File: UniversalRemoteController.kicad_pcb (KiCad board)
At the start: 8 copper layers, 92 parts, among them J1 USB_C_Receptacle_USB2.0_16P, J2 Conn_01x03_Pin, U1 USBLC6-2SC6, U2 TPS631000DRLR, U3 BQ25620RYKR, U4 STM32H750IBKx, U5 MAX16054AZT, U6 AP2161W

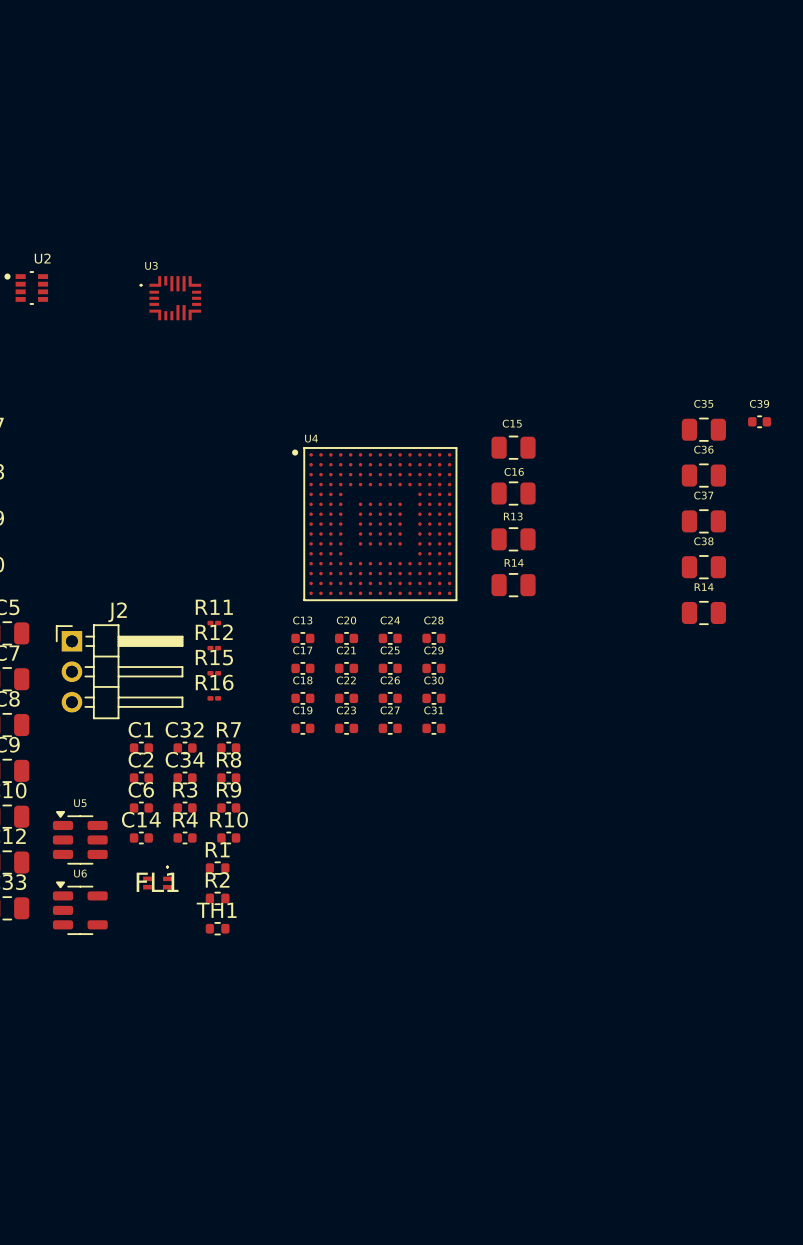
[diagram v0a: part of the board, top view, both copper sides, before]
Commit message: Add the SDRAM ic
16MB SDRAM add
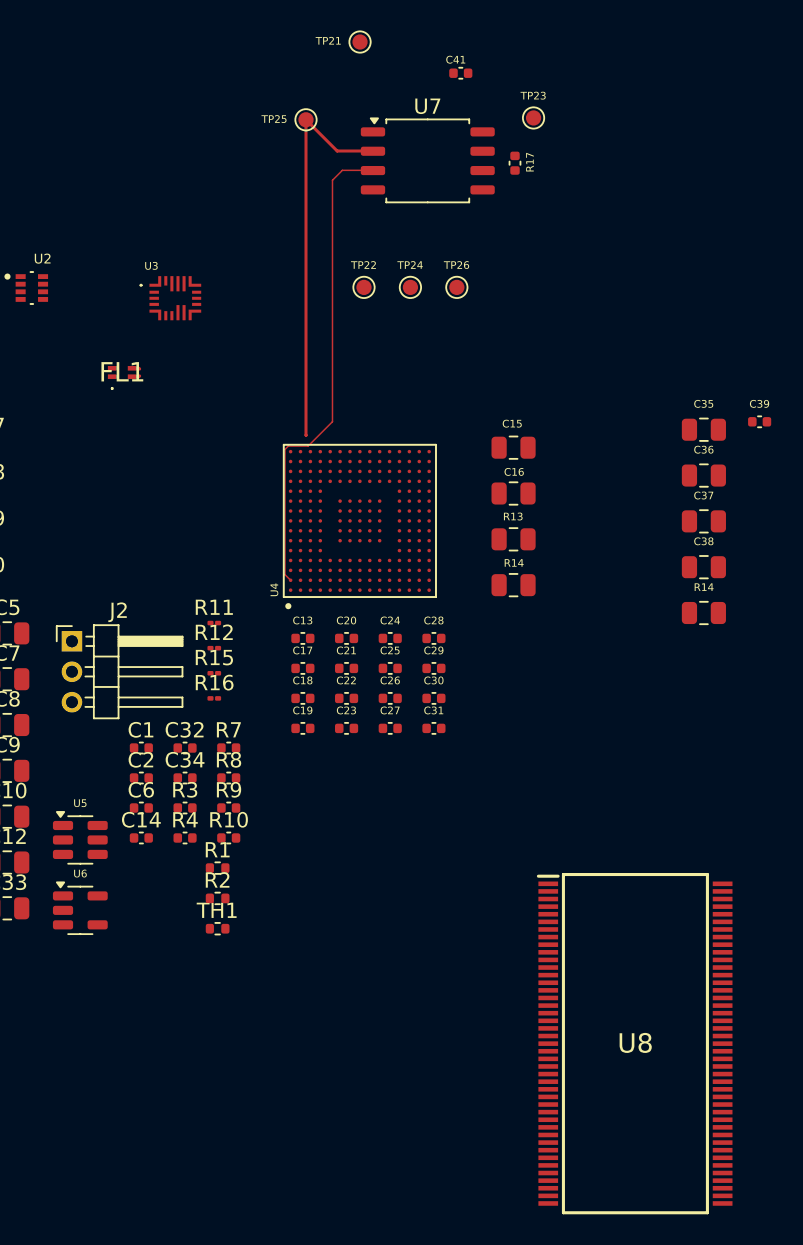
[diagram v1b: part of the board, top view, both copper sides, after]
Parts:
- added C41: 100n, Capacitor_SMD:C_0402_1005Metric, F.Cu at (137.0, 29.2)
- added R17: 10k, Capacitor_SMD:C_0402_1005Metric, F.Cu at (140.5, 35.2)
- added TP21: TestPoint, TestPoint:TestPoint_Pad_D1.0mm, F.Cu at (130.3, 27.2)
- added TP22: TestPoint, TestPoint:TestPoint_Pad_D1.0mm, F.Cu at (130.6, 43.3)
- added TP23: TestPoint, TestPoint:TestPoint_Pad_D1.0mm, F.Cu at (141.8, 32.2)
- added TP24: TestPoint, TestPoint:TestPoint_Pad_D1.0mm, F.Cu at (133.7, 43.3)
- added TP25: TestPoint, TestPoint:TestPoint_Pad_D1.0mm, F.Cu at (126.8, 32.3)
- added TP26: TestPoint, TestPoint:TestPoint_Pad_D1.0mm, F.Cu at (136.7, 43.3)
- added U7: W25Q128JVS, UniversalRemoteControllerLibrary:SOIC-8_5.23x5.23mm_P1.27mm, F.Cu at (134.8, 35.0)
- added U8: IS42S32400F-6TLI, UniversalRemoteControllerLibrary:SOP50P1176X120-86N, F.Cu at (148.4, 93.0)
- moved FL1 33.6 mm to (114.7, 48.9), turned to 180 degrees
- moved U4 1.36 mm to (130.3, 58.7), turned to 90 degrees
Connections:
- FL1 pad 2: /Power/P1_USB_D- -> /MCU/P1_USB_D-
- FL1 pad 3: /Power/P1_USB_D+ -> /MCU/P1_USB_D+
- U4 pad A2: unconnected-(U4-PE2-PadA2) -> /MCU/QUADSPI_BK1_IO2
- U4 pad B14: unconnected-(U4-PC10-PadB14) -> /MCU/QUADSPI_BK1_IO1
- U4 pad B15: unconnected-(U4-PA12-PadB15) -> /MCU/P1_USB_D+
- U4 pad B4: unconnected-(U4-PB9-PadB4) -> /MCU/FMC_A6
- U4 pad B5: unconnected-(U4-PB7-PadB5) -> /MCU/FMC_A11
- U4 pad B6: unconnected-(U4-PB6-PadB6) -> /MCU/QUADSPI_BK1_NCS
- U4 pad C15: unconnected-(U4-PA11-PadC15) -> /MCU/P1_USB_D-
- U4 pad F14: unconnected-(U4-PC9-PadF14) -> /MCU/QUADSPI_BK1_IO0
- U4 pad K2: unconnected-(U4-PF6-PadK2) -> /MCU/QUADSPI_BK1_IO3
- U4 pad L1: unconnected-(U4-PF10-PadL1) -> /MCU/QUADSPI_CLK
- U4 pad P12: unconnected-(U4-PB12-PadP12) -> Net-(U4-PB11)
- U4 pad P13: unconnected-(U4-PB13-PadP13) -> /MCU/FMC_A1
- U4 pad R13: unconnected-(U4-PB11-PadR13) -> Net-(U4-PB11)
- U4 pad R14: unconnected-(U4-PB14-PadR14) -> /MCU/FMC_A0
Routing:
- net /MCU/QUADSPI_BK1_IO2: track 0.00 -> 31.1 mm
- net /MCU/QUADSPI_BK1_IO1: track 0.00 -> 25.5 mm
- net /MCU/P1_USB_D-: track 0.00 -> 0.51 mm
- net /MCU/P1_USB_D+: track 0.00 -> 0.51 mm

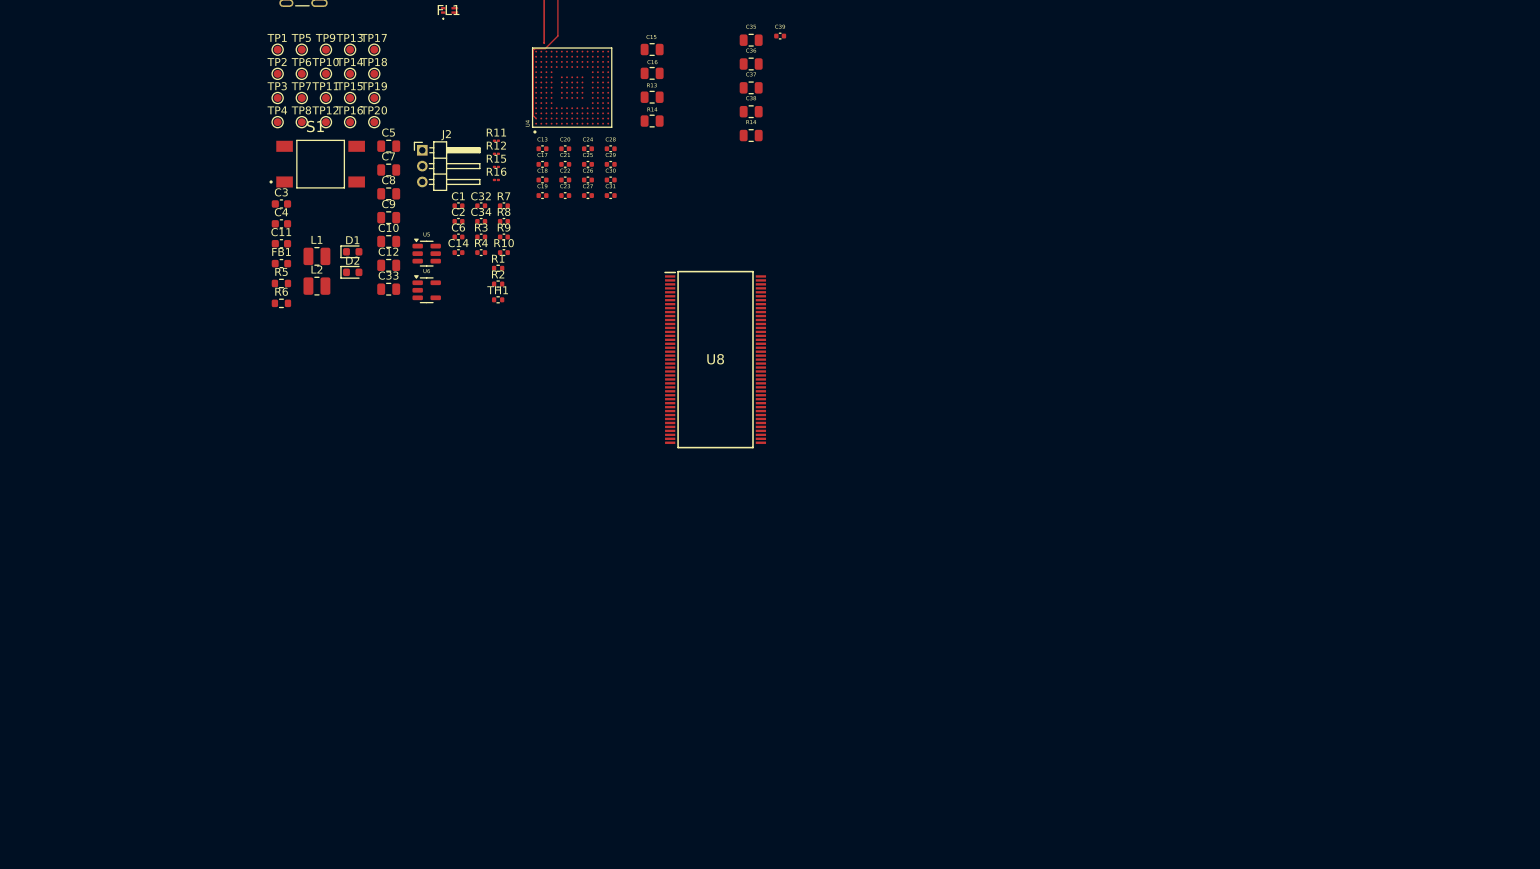
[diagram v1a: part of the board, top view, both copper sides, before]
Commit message: Add the nrf and joystic module
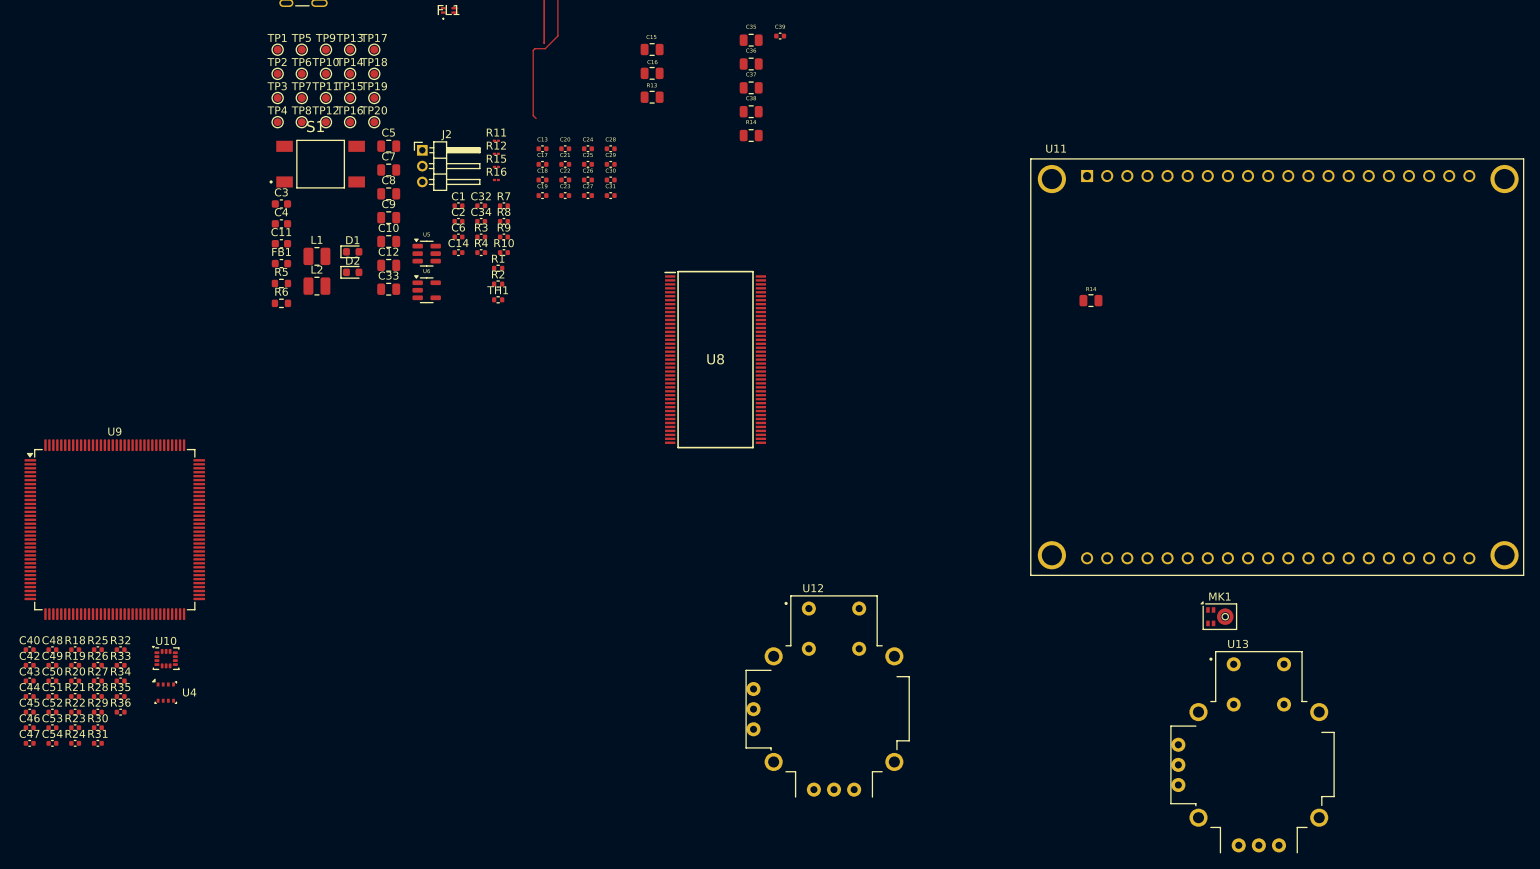
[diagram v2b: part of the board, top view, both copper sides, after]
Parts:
- added C40: 100n, Capacitor_SMD:C_0402_1005Metric, F.Cu at (61.9, 129.6)
- added C42: 100n, Capacitor_SMD:C_0402_1005Metric, F.Cu at (61.9, 131.6)
- added C43: 100n, Capacitor_SMD:C_0402_1005Metric, F.Cu at (61.9, 133.6)
- added C44: 100n, Capacitor_SMD:C_0402_1005Metric, F.Cu at (61.9, 135.5)
- added C45: 100n, Capacitor_SMD:C_0402_1005Metric, F.Cu at (61.9, 137.5)
- added C46: 100n, Capacitor_SMD:C_0402_1005Metric, F.Cu at (61.9, 139.5)
- added C47: 100n, Capacitor_SMD:C_0402_1005Metric, F.Cu at (61.9, 141.4)
- added C48: 100n, Capacitor_SMD:C_0402_1005Metric, F.Cu at (64.7, 129.6)
- added C49: 100n, Capacitor_SMD:C_0402_1005Metric, F.Cu at (64.7, 131.6)
- added C50: 100n, Capacitor_SMD:C_0402_1005Metric, F.Cu at (64.7, 133.6)
- added C51: 100n, Capacitor_SMD:C_0402_1005Metric, F.Cu at (64.7, 135.5)
- added C52: 100n, Capacitor_SMD:C_0402_1005Metric, F.Cu at (64.7, 137.5)
- added C53: 100n, Capacitor_SMD:C_0402_1005Metric, F.Cu at (64.7, 139.5)
- added C54: 100n, Capacitor_SMD:C_0402_1005Metric, F.Cu at (64.7, 141.4)
- added MK1: IM69D130, Sensor_Audio:Infineon_PG-LLGA-5-1, F.Cu at (212.1, 125.5)
- added R18: 10k, Capacitor_SMD:C_0402_1005Metric, F.Cu at (67.6, 129.6)
- added R19: 10k, Capacitor_SMD:C_0402_1005Metric, F.Cu at (67.6, 131.6)
- added R20: 10k, Capacitor_SMD:C_0402_1005Metric, F.Cu at (67.6, 133.6)
- added R21: 10k, Capacitor_SMD:C_0402_1005Metric, F.Cu at (67.6, 135.5)
- added R22: 10k, Capacitor_SMD:C_0402_1005Metric, F.Cu at (67.6, 137.5)
- added R23: 10k, Capacitor_SMD:C_0402_1005Metric, F.Cu at (67.6, 139.5)
- added R24: 10k, Capacitor_SMD:C_0402_1005Metric, F.Cu at (67.6, 141.4)
- added R25: 10k, Capacitor_SMD:C_0402_1005Metric, F.Cu at (70.5, 129.6)
- added R26: 10k, Capacitor_SMD:C_0402_1005Metric, F.Cu at (70.5, 131.6)
- added R27: 10k, Capacitor_SMD:C_0402_1005Metric, F.Cu at (70.5, 133.6)
- added R28: 10k, Capacitor_SMD:C_0402_1005Metric, F.Cu at (70.5, 135.5)
- added R29: 10k, Capacitor_SMD:C_0402_1005Metric, F.Cu at (70.5, 137.5)
- added R30: 10k, Capacitor_SMD:C_0402_1005Metric, F.Cu at (70.5, 139.5)
- added R31: 10k, Capacitor_SMD:C_0402_1005Metric, F.Cu at (70.5, 141.4)
- added R32: 10k, Capacitor_SMD:C_0402_1005Metric, F.Cu at (73.3, 129.6)
- added R33: 10k, Capacitor_SMD:C_0402_1005Metric, F.Cu at (73.3, 131.6)
- added R34: 10k, Capacitor_SMD:C_0402_1005Metric, F.Cu at (73.3, 133.6)
- added R35: 10k, Capacitor_SMD:C_0402_1005Metric, F.Cu at (73.3, 135.5)
- added R36: 10k, Capacitor_SMD:C_0402_1005Metric, F.Cu at (73.3, 137.5)
- added U10: LSM6DSVTR, Package_LGA:LGA-14_3x2.5mm_P0.5mm_LayoutBorder3x4y, F.Cu at (79.1, 130.8)
- added U11: ADAFRUIT2478, UniversalRemoteControllerLibrary:ADAFRUIT_2478, F.Cu at (219.5, 94.0)
- added U12: JOYSTIC-09032, UniversalRemoteControllerLibrary:XDCR_COM-09032, F.Cu at (163.4, 137.1)
- added U13: JOYSTIC-09032, UniversalRemoteControllerLibrary:XDCR_COM-09032, F.Cu at (217.0, 144.2)
- added U9: STM32H750ZBTx, Package_QFP:LQFP-144_20x20mm_P0.5mm, F.Cu at (72.6, 114.5)
- U4: value STM32H750IBKx -> BME280; footprint UniversalRemoteControllerLibrary:BGA201C65P15X15_1000X1000X60 -> Package_LGA:Bosch_LGA-8_2.5x2.5mm_P0.65mm_ClockwisePinNumbering
- moved U4 92.0 mm to (79.0, 135.0), turned to 0 degrees
- moved R14 59.9 mm to (195.8, 85.5)
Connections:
- net /Power/BATT_FET_FLAG renamed /MCU/BATT_FET_FLAG
- net /Power/BQ25620_SCK renamed /MCU/I2C_SCK
- net /Power/BQ25620_SDA renamed /MCU/I2C_SDA
- net /Power/~{BQ25620_CE} renamed /MCU/~{BQ25620_CE}
- net /Power/~{BQ25620_INT} renamed /MCU/~{BQ25620_INT}
- C13 pad 1: Net-(U4-NRST) -> Net-(U9-NRST)
- R13 pad 2: Net-(U4-NRST) -> Net-(U9-NRST)
- R14 pad 2: Net-(U4-BOOT0) -> Net-(U9-BOOT0)
- U8 pad 1: unconnected-(U8-VDD_1-Pad1) -> Net-(U8-VDD_1)
- U8 pad 10: unconnected-(U8-DQ5-Pad10) -> /MCU/FMC_DQ5
- U8 pad 11: unconnected-(U8-DQ6-Pad11) -> /MCU/FMC_DQ6
- U8 pad 12: unconnected-(U8-VSSQ_2-Pad12) -> GND
- U8 pad 13: unconnected-(U8-DQ7-Pad13) -> /MCU/FMC_DQ7
- U8 pad 15: unconnected-(U8-VDD_2-Pad15) -> Net-(U8-VDD_2)
- U8 pad 16: unconnected-(U8-DQM0-Pad16) -> /MCU/FMC_NBL0
- U8 pad 17: unconnected-(U8-~{WE}-Pad17) -> /MCU/FMC_SDNWE
- U8 pad 18: unconnected-(U8-~{CAS}-Pad18) -> /MCU/FMC_SDNCAS
- U8 pad 19: unconnected-(U8-~{RAS}-Pad19) -> /MCU/FMC_SDNRAS
- U8 pad 2: unconnected-(U8-DQ0-Pad2) -> /MCU/FMC_DQ0
- U8 pad 20: unconnected-(U8-~{CS}-Pad20) -> /MCU/FMC_SDNE0
- U8 pad 22: unconnected-(U8-BA0-Pad22) -> /MCU/FMC_BA0
- U8 pad 23: unconnected-(U8-BA1-Pad23) -> /MCU/FMC_BA1
- U8 pad 28: unconnected-(U8-DQM2-Pad28) -> Net-(U8-DQM2)
- U8 pad 29: unconnected-(U8-VDD_3-Pad29) -> Net-(U8-VDD_3)
- U8 pad 3: unconnected-(U8-VDDQ_1-Pad3) -> Net-(U8-VDDQ_1)
- U8 pad 31: unconnected-(U8-DQ16-Pad31) -> Net-(U8-DQ16)
- U8 pad 32: unconnected-(U8-VSSQ_3-Pad32) -> Net-(U8-VSSQ_3)
- U8 pad 33: unconnected-(U8-DQ17-Pad33) -> Net-(U8-DQ17)
- U8 pad 34: unconnected-(U8-DQ18-Pad34) -> Net-(U8-DQ18)
- U8 pad 35: unconnected-(U8-VDDQ_3-Pad35) -> Net-(U8-VDDQ_3)
- U8 pad 36: unconnected-(U8-DQ19-Pad36) -> Net-(U8-DQ19)
- U8 pad 37: unconnected-(U8-DQ20-Pad37) -> Net-(U8-DQ20)
- U8 pad 38: unconnected-(U8-VSSQ_4-Pad38) -> Net-(U8-VSSQ_4)
- U8 pad 39: unconnected-(U8-DQ21-Pad39) -> Net-(U8-DQ21)
- U8 pad 4: unconnected-(U8-DQ1-Pad4) -> /MCU/FMC_DQ1
- U8 pad 40: unconnected-(U8-DQ22-Pad40) -> Net-(U8-DQ22)
- U8 pad 41: unconnected-(U8-VDDQ_4-Pad41) -> Net-(U8-VDDQ_4)
- U8 pad 42: unconnected-(U8-DQ23-Pad42) -> Net-(U8-DQ23)
- U8 pad 43: unconnected-(U8-VDD_4-Pad43) -> Net-(U8-VDD_4)
- U8 pad 44: unconnected-(U8-VSS_1-Pad44) -> GND
- U8 pad 45: unconnected-(U8-DQ24-Pad45) -> Net-(U8-DQ24)
- U8 pad 46: unconnected-(U8-VSSQ_5-Pad46) -> GND
- U8 pad 47: unconnected-(U8-DQ25-Pad47) -> Net-(U8-DQ25)
- U8 pad 48: unconnected-(U8-DQ26-Pad48) -> Net-(U8-DQ26)
- U8 pad 49: unconnected-(U8-VDDQ_5-Pad49) -> Net-(U8-VDDQ_5)
- U8 pad 5: unconnected-(U8-DQ2-Pad5) -> /MCU/FMC_DQ2
- U8 pad 50: unconnected-(U8-DQ27-Pad50) -> Net-(U8-DQ27)
- U8 pad 51: unconnected-(U8-DQ28-Pad51) -> Net-(U8-DQ28)
- U8 pad 52: unconnected-(U8-VSSQ_6-Pad52) -> Net-(U8-VSSQ_6)
- U8 pad 53: unconnected-(U8-DQ29-Pad53) -> Net-(U8-DQ29)
- U8 pad 54: unconnected-(U8-DQ30-Pad54) -> Net-(U8-DQ30)
- U8 pad 55: unconnected-(U8-VDDQ_6-Pad55) -> Net-(U8-VDDQ_6)
- U8 pad 56: unconnected-(U8-DQ31-Pad56) -> Net-(U8-DQ31)
- U8 pad 58: unconnected-(U8-VSS_2-Pad58) -> GND
- U8 pad 59: unconnected-(U8-DQM3-Pad59) -> Net-(U8-DQM3)
- U8 pad 6: unconnected-(U8-VSSQ_1-Pad6) -> GND
- U8 pad 67: unconnected-(U8-CKE-Pad67) -> /MCU/FMC_SDCKE
- U8 pad 68: unconnected-(U8-CLK-Pad68) -> /MCU/FMC_SDCLK
- U8 pad 7: unconnected-(U8-DQ3-Pad7) -> /MCU/FMC_DQ3
- U8 pad 71: unconnected-(U8-DQM1-Pad71) -> /MCU/FMC_NBL1
- U8 pad 72: unconnected-(U8-VSS_3-Pad72) -> GND
- U8 pad 74: unconnected-(U8-DQ8-Pad74) -> /MCU/FMC_DQ8
- U8 pad 75: unconnected-(U8-VDDQ_7-Pad75) -> Net-(U8-VDDQ_7)
- U8 pad 76: unconnected-(U8-DQ9-Pad76) -> /MCU/FMC_DQ9
- U8 pad 77: unconnected-(U8-DQ10-Pad77) -> /MCU/FMC_DQ10
- U8 pad 78: unconnected-(U8-VSSQ_7-Pad78) -> GND
- U8 pad 79: unconnected-(U8-DQ11-Pad79) -> /MCU/FMC_DQ11
- U8 pad 8: unconnected-(U8-DQ4-Pad8) -> /MCU/FMC_DQ4
- U8 pad 80: unconnected-(U8-DQ12-Pad80) -> /MCU/FMC_DQ12
- U8 pad 81: unconnected-(U8-VDDQ_8-Pad81) -> Net-(U8-VDDQ_8)
- U8 pad 82: unconnected-(U8-DQ13-Pad82) -> /MCU/FMC_DQ13
- U8 pad 83: unconnected-(U8-DQ14-Pad83) -> /MCU/FMC_DQ14
- U8 pad 84: unconnected-(U8-VSSQ_8-Pad84) -> GND
- U8 pad 85: unconnected-(U8-DQ15-Pad85) -> /MCU/FMC_DQ15
- U8 pad 86: unconnected-(U8-VSS_4-Pad86) -> GND
- U8 pad 9: unconnected-(U8-VDDQ_2-Pad9) -> Net-(U8-VDDQ_2)
